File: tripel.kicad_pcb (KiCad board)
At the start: 2 copper layers, 95.1 x 95.2 mm, 85 parts, among them J1 Left Columns, J10 Right Reset, J11 Left Reset, J12 Far Left Rows, J13 Far Left Rows, J2 Left Rows, J3 Right Rows, J4 Right Columns, J5 Left Rows, J6 USB_mini_micro_B, J7 Conn_01x04, J8 Right Rows, J9 Reset, K1.1 KEYSW, K1.2 KEYSW, K1.3 KEYSW, K1.4 KEYSW, K1.4_2u1 KEYSW, K1.5 KEYSW, K2.1 KEYSW, K2.2 KEYSW, K2.2_1.5u1 KEYSW, K2.3 KEYSW, K2.4 KEYSW, K2.4_1.5u1 KEYSW, K2.5 KEYSW, K3.1 KEYSW, K3.2 KEYSW, K3.2_1.75u1 KEYSW, K3.3 KEYSW, K3.3_2.25u1 KEYSW, K3.4 KEYSW, K3.5 KEYSW, K4.1 KEYSW, K4.2 KEYSW, K4.2_1.75u1 KEYSW, K4.3 KEYSW, K4.3_2.25u1 KEYSW, K4.4 KEYSW, K4.5 KEYSW, K5.1_1.5u1 KEYSW, K5.1_1u1 KEYSW, K5.1_1u2 KEYSW, K5.2_1.5u1 KEYSW, K5.2_1u1 KEYSW, K5.2_1u2 KEYSW, K5.3_1.5u1 KEYSW, K5.3_1u1 KEYSW, K5.3_7u1 KEYSW, K5.4_1.5u1 KEYSW, K5.4_1u1 KEYSW, U1 ProMicro_ChipSideDown

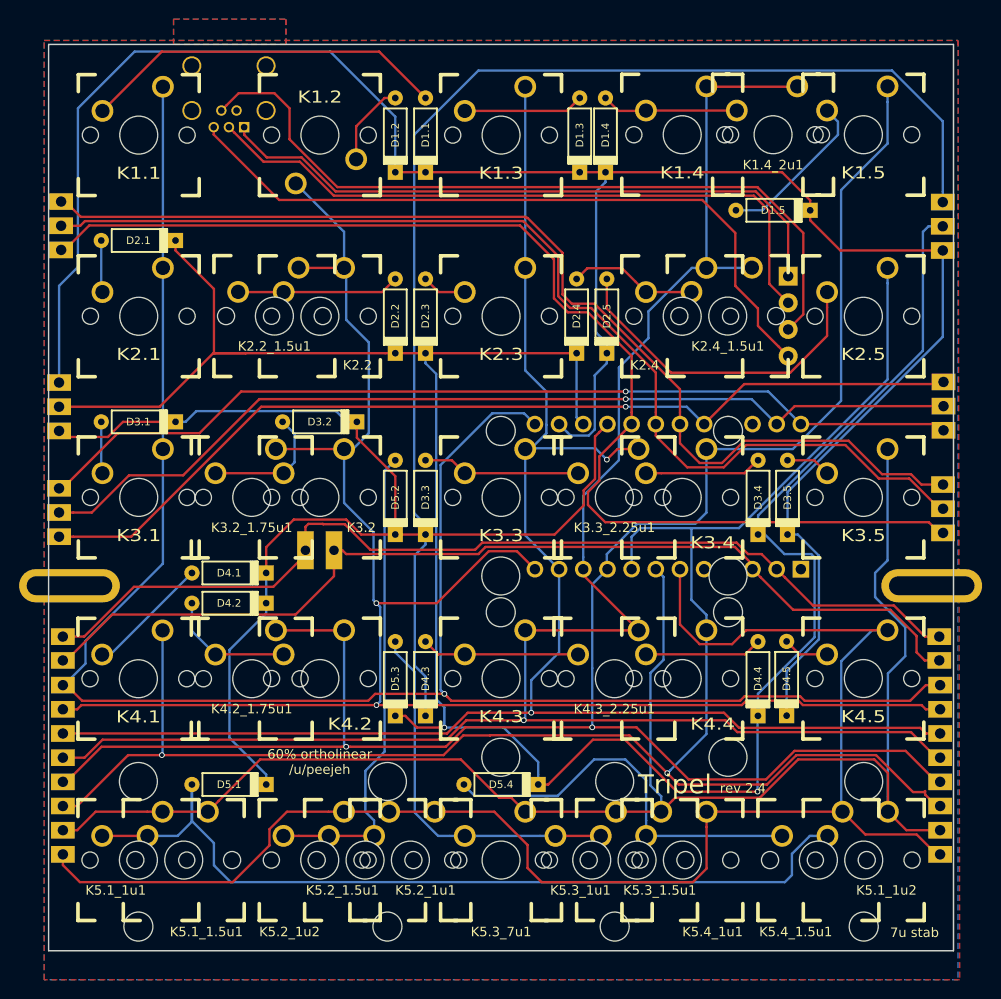
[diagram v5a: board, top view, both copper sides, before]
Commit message: Add split right shift and 1.75u enter options
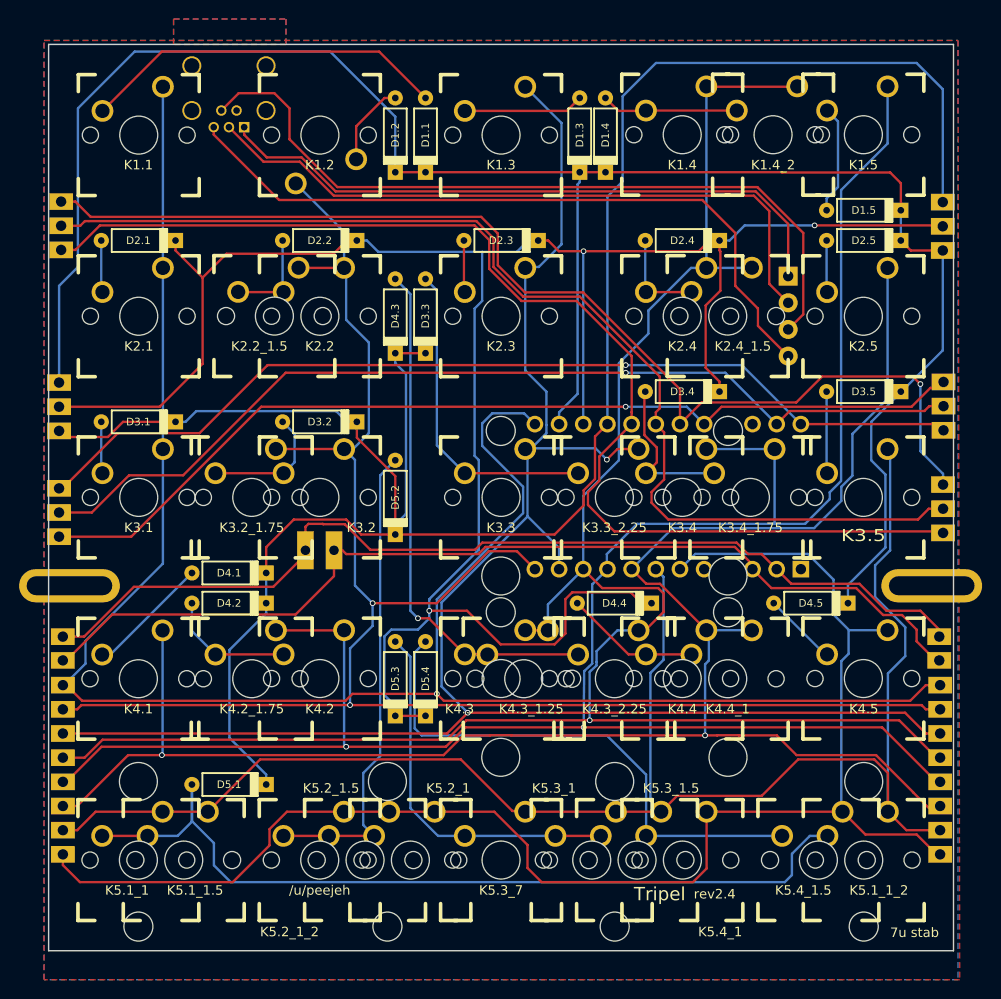
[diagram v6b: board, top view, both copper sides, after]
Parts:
- added K3.4_1.75: KEYSW, keyboard:MX_PCB_175H, F.Cu at (185.6, 85.7)
- added K4.3_1.25: KEYSW, keyboard:MX_PCB_125H, F.Cu at (161.8, 104.7)
- added K4.4_1: KEYSW, keyboard:MX, F.Cu at (183.2, 104.7)
- moved D4.3 38.2 mm to (148.3, 66.6)
- moved D2.5 28.1 mm to (197.5, 58.7), turned to 180 degrees
- moved D3.3 19.0 mm to (151.4, 66.6)
- moved D4.4 17.0 mm to (171.3, 96.8), turned to 180 degrees
- moved D3.5 13.7 mm to (197.5, 74.6), turned to 180 degrees
- moved D3.4 13.7 mm to (178.4, 74.6), turned to 180 degrees
- moved D2.4 13.7 mm to (178.4, 58.7), turned to 180 degrees
- moved D5.4 13.7 mm to (151.4, 104.7), turned to 90 degrees
- moved D2.2 11.2 mm to (140.3, 58.7), turned to 180 degrees
- moved D2.3 11.2 mm to (159.4, 58.7), turned to 180 degrees
- moved D1.5 9.53 mm to (197.5, 55.5)
- moved D4.5 8.32 mm to (191.9, 96.8), turned to 180 degrees
- renumbered K1.4_2u1 to K1.4_2, K2.2_1.5u1 to K2.2_1.5, K2.4_1.5u1 to K2.4_1.5, K3.2_1.75u1 to K3.2_1.75, K3.3_2.25u1 to K3.3_2.25, K4.2_1.75u1 to K4.2_1.75, K4.3_2.25u1 to K4.3_2.25, K5.1_1u1 to K5.1_1, K5.1_1.5u1 to K5.1_1.5, K5.1_1u2 to K5.1_1_2, K5.2_1u1 to K5.2_1, K5.2_1.5u1 to K5.2_1.5, K5.2_1u2 to K5.2_1_2, K5.3_1u1 to K5.3_1, K5.3_1.5u1 to K5.3_1.5, K5.3_7u1 to K5.3_7, K5.4_1u1 to K5.4_1, K5.4_1.5u1 to K5.4_1.5
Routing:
- net Net-(D4.3-Pad2): track 16.6 -> 55.0 mm, vias 0 -> 1
- net Net-(D2.5-Pad2): track 35.2 -> 5.44 mm
- net Net-(D3.1-Pad1): track 252.3 -> 227.2 mm
- net Net-(D1.1-Pad1): track 228.2 -> 208.4 mm
- net Net-(D3.3-Pad2): track 16.6 -> 34.0 mm
- net Net-(J1-Pad4): track 208.0 -> 222.5 mm
- net Net-(D5.4-Pad2): track 42.3 -> 56.6 mm
- net Net-(J1-Pad6): track 177.5 -> 190.6 mm
- net Net-(J1-Pad5): track 197.0 -> 204.8 mm
- net Net-(D2.2-Pad2): track 17.1 -> 10.3 mm
- net Net-(D2.1-Pad1): track 243.4 -> 236.7 mm, vias 2 -> 3
- net Net-(D1.5-Pad2): track 17.0 -> 11.4 mm
- net Net-(J12-Pad3): track 112.8 -> 118.0 mm, vias 0 -> 1
- net Net-(D3.4-Pad2): track 12.3 -> 16.8 mm
- net Net-(J12-Pad2): track 113.7 -> 117.8 mm
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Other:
- board text added: "/u/peejeh"
- board text added: "rev2.4"
- board text removed: "60% ortholinear /u/peejeh"
- board text removed: "rev 2.4"

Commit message: Add stab holes for 2u backspace
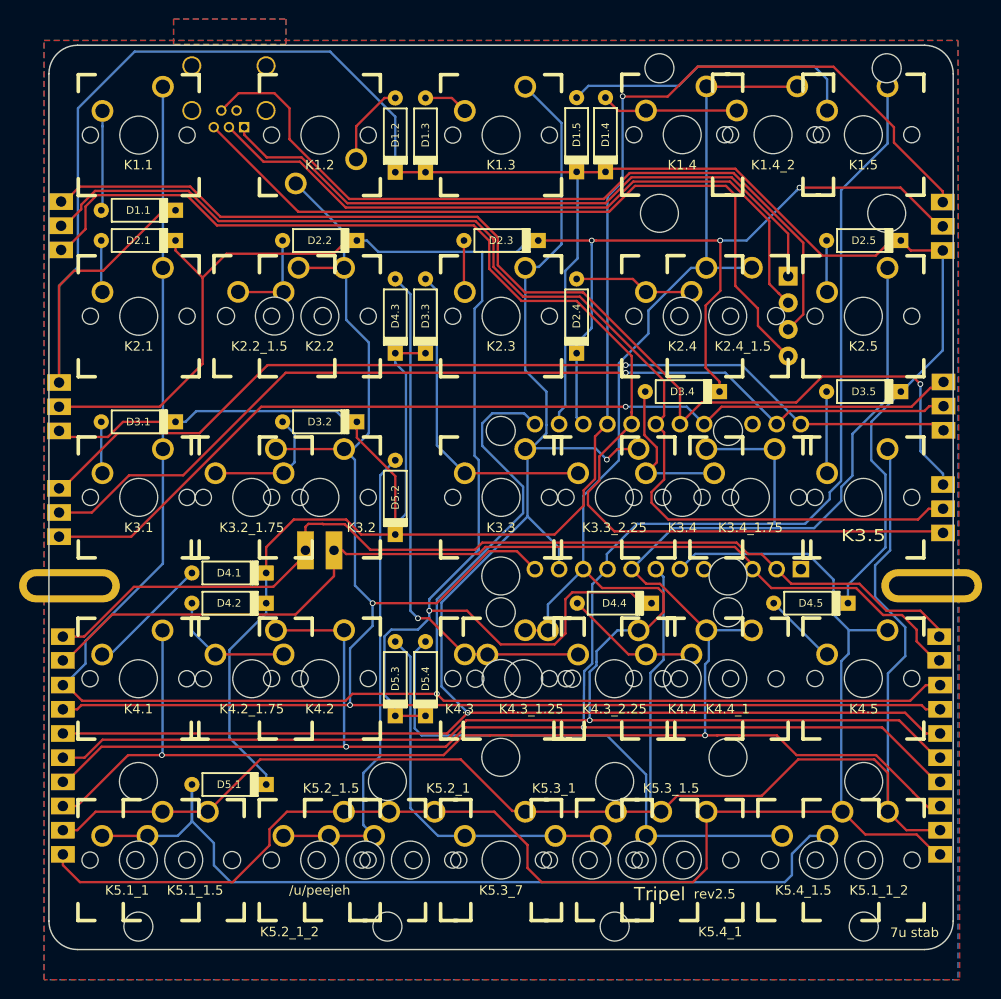
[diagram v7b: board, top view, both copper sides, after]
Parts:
- K1.4_2: footprint keyboard:MX -> keyboard:MX_PCB_200H
- moved D1.5 31.2 mm to (167.3, 47.6), turned to 90 degrees
- moved D1.1 31.2 mm to (121.3, 55.5), turned to 180 degrees
- moved D1.3 16.2 mm to (151.4, 47.6)
- moved D2.4 13.7 mm to (167.3, 66.6), turned to 90 degrees
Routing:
- net Net-(D1.1-Pad2): track 38.5 -> 10.5 mm
- net Net-(D1.1-Pad1): track 208.4 -> 232.4 mm
- net Net-(D1.5-Pad2): track 11.4 -> 31.5 mm
- net Net-(D1.3-Pad2): track 12.6 -> 4.69 mm
- net Net-(D3.1-Pad1): track 227.2 -> 221.5 mm, vias 0 -> 1
- net Net-(D2.1-Pad1): track 236.7 -> 241.2 mm, vias 3 -> 4
- net Net-(J6-Pad1): track 75.1 -> 79.2 mm
- net Net-(J12-Pad1): track 124.5 -> 128.5 mm
- net Net-(J12-Pad2): track 117.8 -> 121.0 mm
- net Net-(D2.4-Pad2): track 10.2 -> 12.6 mm
- net Net-(J6-Pad5): track 67.3 -> 69.0 mm
- net Net-(J6-Pad3): track 70.9 -> 72.5 mm
- net Net-(J6-Pad2): track 80.7 -> 82.3 mm
- net Net-(J12-Pad3): track 118.0 -> 119.1 mm
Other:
- board size 95.1 x 95.2 mm -> 95 x 95 mm
- board text added: "rev2.5"
- board text removed: "rev2.4"

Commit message: Move inter-PCB contacts away from PCB edge to help prevent shorts
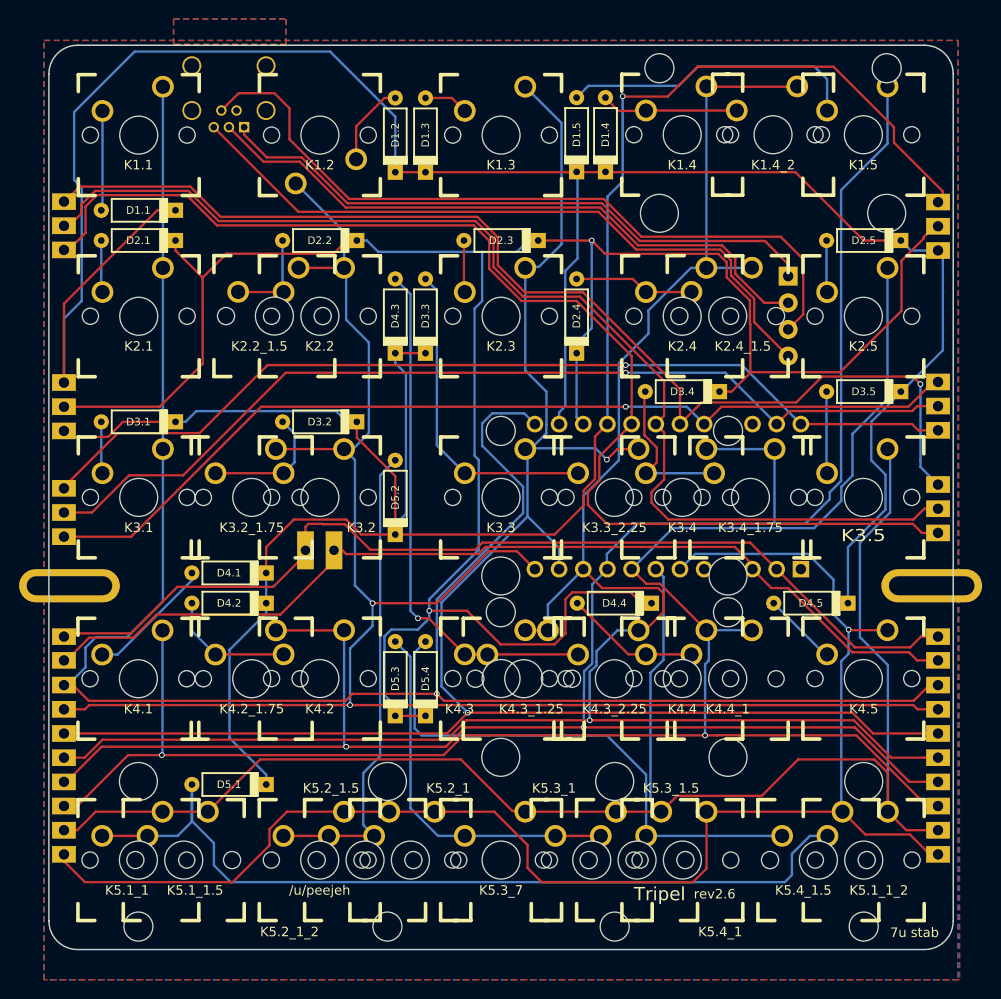
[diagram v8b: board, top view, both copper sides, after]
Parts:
- moved J2 0.58 mm to (205.3, 76.1)
- moved J12 0.53 mm to (205.3, 86.9)
- moved J13 0.52 mm to (113.5, 87.3)
- moved J8 0.52 mm to (113.5, 76.2)
- moved J5 0.50 mm to (205.3, 57.2)
- moved J3 0.30 mm to (113.5, 57.1)
- moved J4 0.22 mm to (205.3, 114.3)
- moved J11 0.13 mm to (205.3, 101.6)
- moved J10 0.12 mm to (113.5, 101.6)
- moved J1 0.11 mm to (113.5, 114.3)
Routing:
- net Net-(J6-Pad1): track 79.2 -> 72.7 mm
- net Net-(J6-Pad3): track 72.5 -> 67.3 mm
- net Net-(J6-Pad5): track 69.0 -> 64.8 mm
- net Net-(J6-Pad2): track 82.3 -> 79.0 mm
- net Net-(D1.1-Pad1): track 232.4 -> 229.6 mm
- net Net-(D2.1-Pad1): track 241.2 -> 243.7 mm, vias 4 -> 2
- net Net-(J10-Pad2): track 104.9 -> 103.0 mm
- net Net-(J1-Pad8): track 201.8 -> 203.5 mm
- net Net-(J13-Pad2): track 102.0 -> 100.9 mm
- net Net-(J13-Pad1): track 101.2 -> 100.1 mm
- net Net-(J1-Pad1): track 158.4 -> 157.8 mm, vias 0 -> 1
- net Net-(J12-Pad2): track 121.0 -> 120.5 mm
- net Net-(J1-Pad2): track 173.0 -> 172.5 mm
- net Net-(J12-Pad3): track 119.1 -> 118.5 mm
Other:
- board text added: "rev2.6"
- board text removed: "rev2.5"
